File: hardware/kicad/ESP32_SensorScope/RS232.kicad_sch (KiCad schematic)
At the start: 17 parts, among them U10 MAX232, U11 SN74LV1T125DBV, U12 OPA333xxDBV, U9 SN74LV1T125DBV

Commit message: Various changes
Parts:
- removed U12: OPA333xxDBV, Package_TO_SOT_SMD:SOT-23-5, symbol Amplifier_Operational:OPA333xxDBV
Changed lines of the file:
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@@
+	(wire
+		(pts
+			(xy 139.7 95.25) (xy 153.67 95.25)
+		)
+		(stroke
+			(width 0)
+			(type default)
+		)
+	)
 	(wire
 		(pts
 			(xy 83.82 111.76) (xy 92.71 111.76)
-		)
-		(stroke
-			(width 0)
-			(type default)
-		)
-	)
-	(wire
-		(pts
-			(xy 139.7 95.25) (xy 153.67 95.25)
 		)
 		(stroke
@@
 					(unit 1)
 				)
-			)
-		)
-	)
-	(symbol
-		(lib_id "Amplifier_Operational:OPA333xxDBV")
-		(at 137.16 144.78 0)
-		(unit 1)
-		(exclude_from_sim no)
-		(in_bom yes)
-		(on_board yes)
-		(dnp no)
-		(property "Reference" "U12"
-			(at 139.446 138.43 0)
-			(effects
-				(font
-					(size 1.27 1.27)
-				)
-			)
-		)
-		(property "Value" "OPA333xxDBV"
-			(at 144.018 140.97 0)
-			(effects
-				(font
-					(size 1.27 1.27)
-				)
-			)
-		)
-		(property "Footprint" "Package_TO_SOT_SMD:SOT-23-5"
-			(at 134.62 149.86 0)
-			(effects
-				(font
-					(size 1.27 1.27)
-				)
-				(justify left)
-				(hide yes)
-			)
-		)
-		(property "Datasheet" "http://www.ti.com/lit/ds/symlink/opa333.pdf"
-			(at 137.16 139.7 0)
-			(effects
-				(font
-					(size 1.27 1.27)
-				)
-				(hide yes)
-			)
-		)
-		(property "Description" "Single 1.8V, microPower, CMOS Operational Amplifiers, Zero-Drift Series, SOT-23-5"
-			(at 137.16 144.78 0)
-			(effects
-				(font
-					(size 1.27 1.27)
-				)
-				(hide yes)
-			)
-		)
-		(pin "2"
-		)
-		(pin "1"
-		)
-		(pin "3"
-		)
-		(pin "4"
-		)
-		(pin "5"
-		)
-		(instances
-			(project "ESP32_SensorScope"
-				(path "/53b18f60-802b-4114-ad1b-2672cfed64a1/61855475-056f-41a1-be83-8f98d1ed07bc"
-					(reference "U12")
-					(unit 1)
-				)

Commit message: something probobly
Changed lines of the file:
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@@
 	(wire
 		(pts
-			(xy 80.01 69.85) (xy 74.93 69.85)
+			(xy 80.01 73.66) (xy 71.12 73.66)
 		)
 		(stroke
@@
 	(wire
 		(pts
-			(xy 96.52 68.58) (xy 88.9 68.58)
+			(xy 96.52 67.31) (xy 59.69 67.31)
 		)
 		(stroke
@@
 	(wire
 		(pts
-			(xy 96.52 80.01) (xy 96.52 68.58)
+			(xy 96.52 80.01) (xy 96.52 67.31)
 		)
 		(stroke
@@
 	(wire
 		(pts
-			(xy 80.01 69.85) (xy 80.01 87.63)
+			(xy 80.01 73.66) (xy 80.01 87.63)
 		)
 		(stroke
@@
 	(global_label "TX"
 		(shape input)
-		(at 88.9 68.58 180)
+		(at 59.69 67.31 180)
 		(fields_autoplaced yes)
 		(effects
@@
 		)
 		(property "Intersheetrefs" "${INTERSHEET_REFS}"
-			(at 83.7377 68.58 0)
+			(at 54.5277 67.31 0)
 			(effects
 				(font
@@
 	(global_label "RS232_RX_nEN"
 		(shape input)
-		(at 74.93 69.85 180)
+		(at 71.12 73.66 180)
 		(fields_autoplaced yes)
 		(effects
@@
 		)
 		(property "Intersheetrefs" "${INTERSHEET_REFS}"
-			(at 57.7936 69.85 0)
+			(at 53.9836 73.66 0)
 			(effects
 				(font

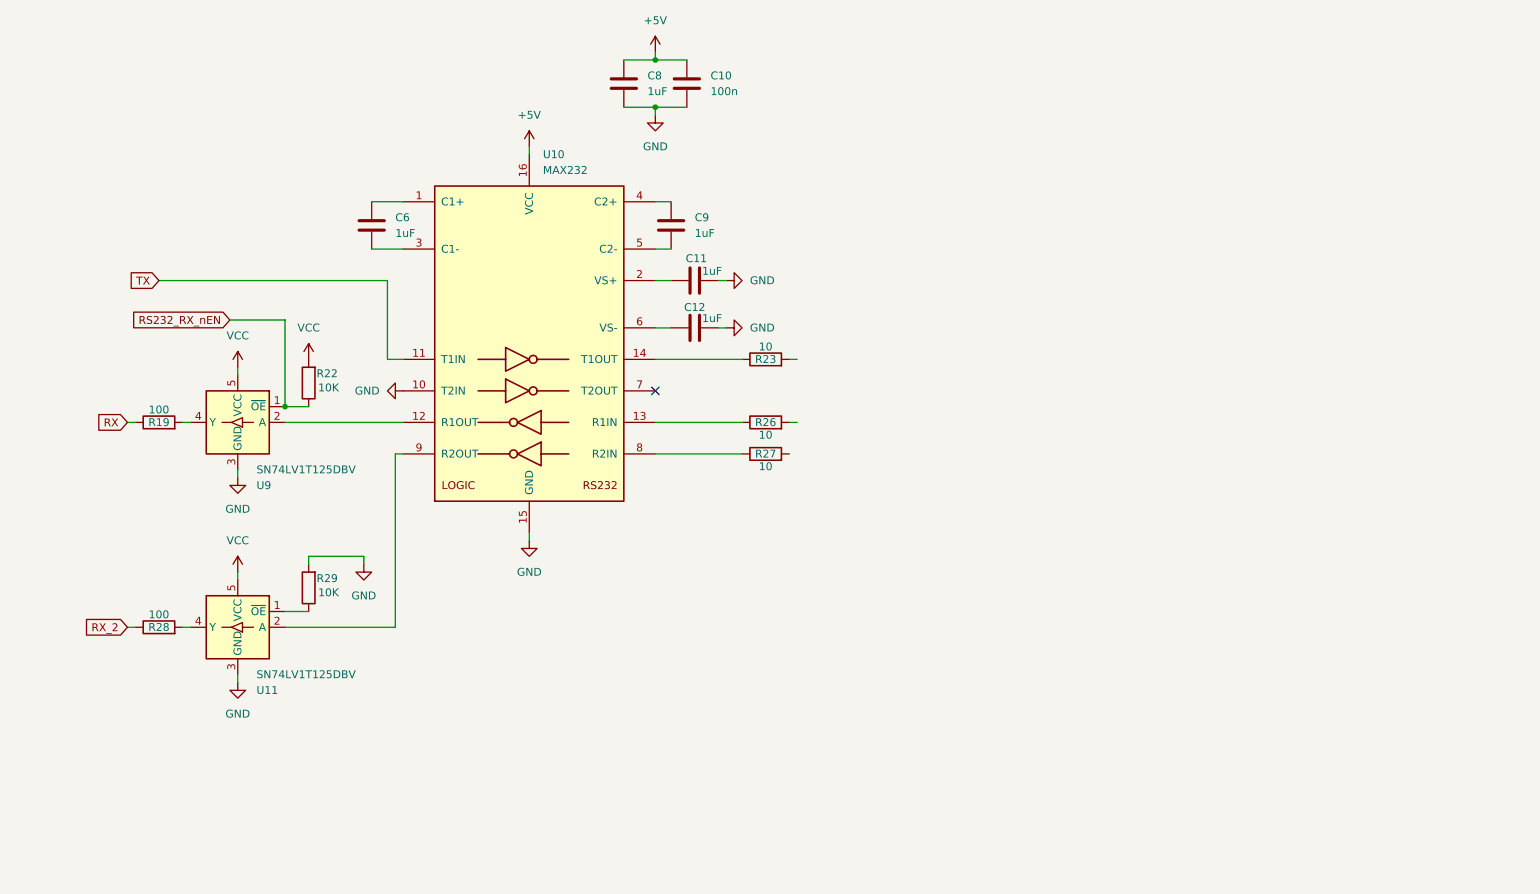
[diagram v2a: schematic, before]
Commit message: som updates on the schematics
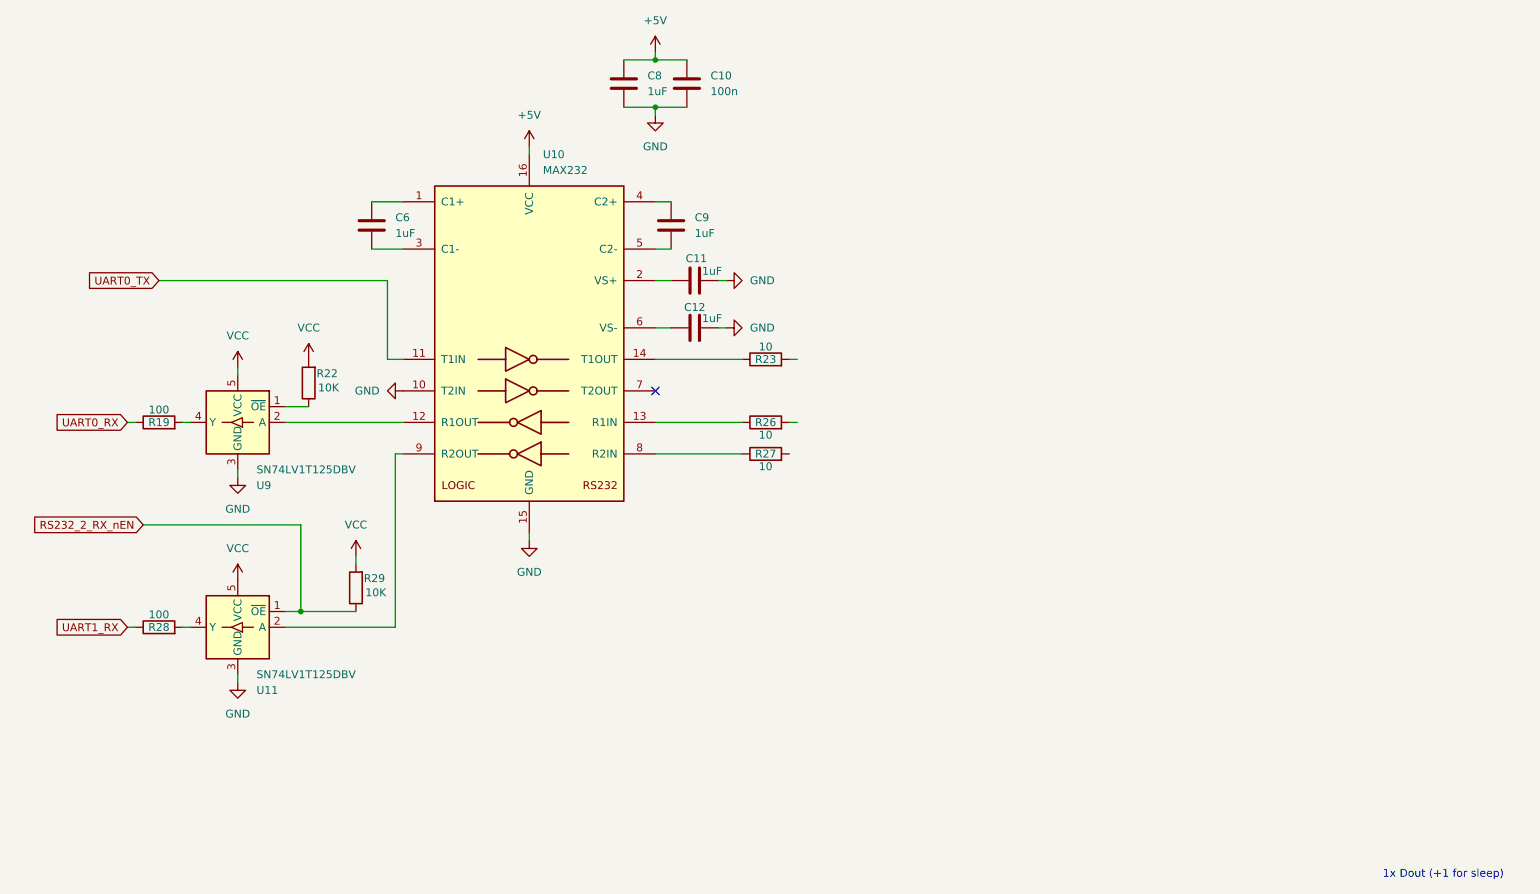
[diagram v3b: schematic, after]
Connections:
- net GND: no longer R29.2
- net VCC: now also R29.2
- net RS232_2_RX_nEN: now reaches R29.1, U11.1 (~{OE})
- net RS232_RX_nEN: no longer names the net of R22.1, U9.1 (~{OE})
- net RX renamed UART0_RX
- net RX_2 renamed UART1_RX
- net TX renamed UART0_TX
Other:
- note added: "1x Dout (+1 for sleep)"
- moved on the sheet: R29

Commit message: updatet schematic
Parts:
- removed R23, R26, R27: 10, symbol Device:R
- added D36, D37, D38: 28VDC, symbol Device:D_TVS
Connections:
- net GND: now also D36.1 (A1), D37.1 (A1), D38.1 (A1)
- net RS232_TX: now reaches U10.14 (T1OUT)
- net RS232_TX: now also D38.2 (A2)
- net RS232_RX1: now reaches U10.13 (R1IN)
- net RS232_RX1: now also D37.2 (A2)
- net RS232_RX2: now reaches U10.8 (R2IN)
- net RS232_RX2: now also D36.2 (A2)

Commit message: addet some footprints"
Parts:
- C10, C11, C12, C6, C8, C9: footprint (none) -> Capacitor_SMD:C_0805_2012Metric
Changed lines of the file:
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@@
 			)
 		)
-		(property "Footprint" ""
+		(property "Footprint" "Capacitor_SMD:C_0805_2012Metric"
 			(at 145.7452 39.37 0)
 			(effects
@@
 			)
 		)
-		(property "Footprint" ""
+		(property "Footprint" "Capacitor_SMD:C_0805_2012Metric"
 			(at 142.24 75.8952 0)
 			(effects
@@
 			)
 		)
-		(property "Footprint" ""
+		(property "Footprint" "Capacitor_SMD:C_0805_2012Metric"
 			(at 135.5852 39.37 0)
 			(effects
@@
 			)
 		)
-		(property "Footprint" ""
+		(property "Footprint" "Capacitor_SMD:C_0805_2012Metric"
 			(at 142.24 68.2752 0)
 			(effects
@@
 			)
 		)
-		(property "Footprint" ""
+		(property "Footprint" "Capacitor_SMD:C_0805_2012Metric"
 			(at 94.9452 62.23 0)
 			(effects
@@
 			)
 		)
-		(property "Footprint" ""
+		(property "Footprint" "Capacitor_SMD:C_0805_2012Metric"
 			(at 143.2052 62.23 0)
 			(effects
